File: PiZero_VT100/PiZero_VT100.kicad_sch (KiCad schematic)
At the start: 32 parts, among them J1 GPIO, J2 RS232, J3 Ext. Power max,. 9V DC/AC, J4 Mini-DIN-6, J5 to Testpins 22(DM) and TP23(D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, J6 USB_A, J7 Z80-MBC2 direct, J8 LCD Power, J9 On / Off, K1 G5V-2, Q1 BC547, U1 LM350_TO220

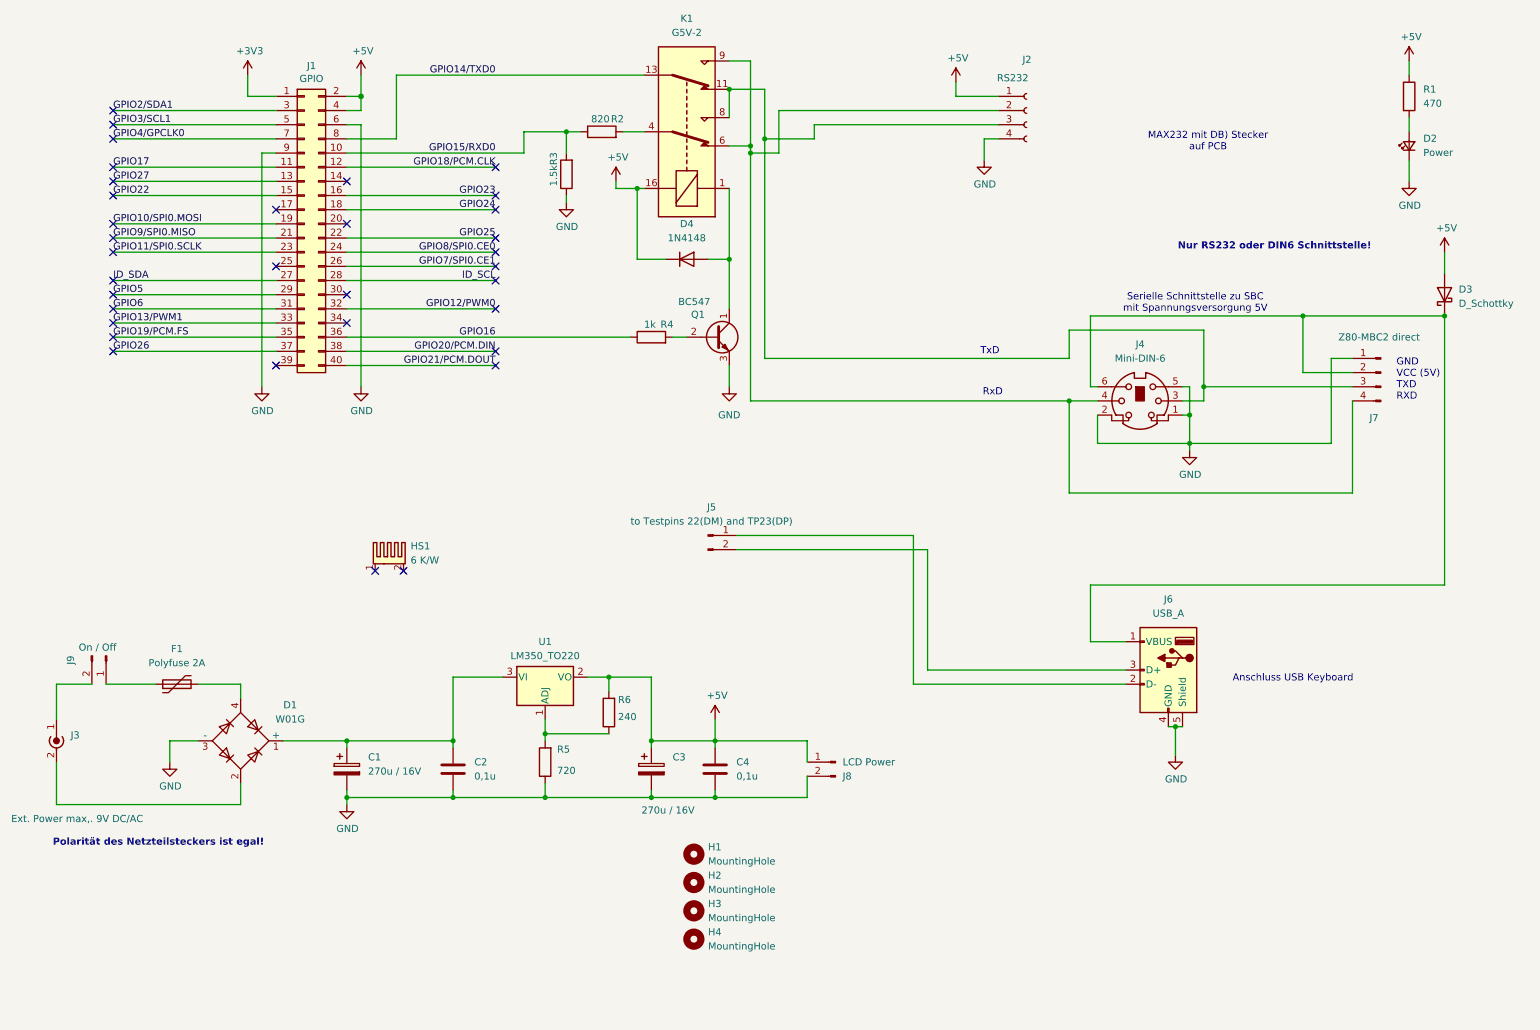
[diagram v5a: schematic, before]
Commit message: Summer berücksichtig Layout für Fertigung bei PCBWays
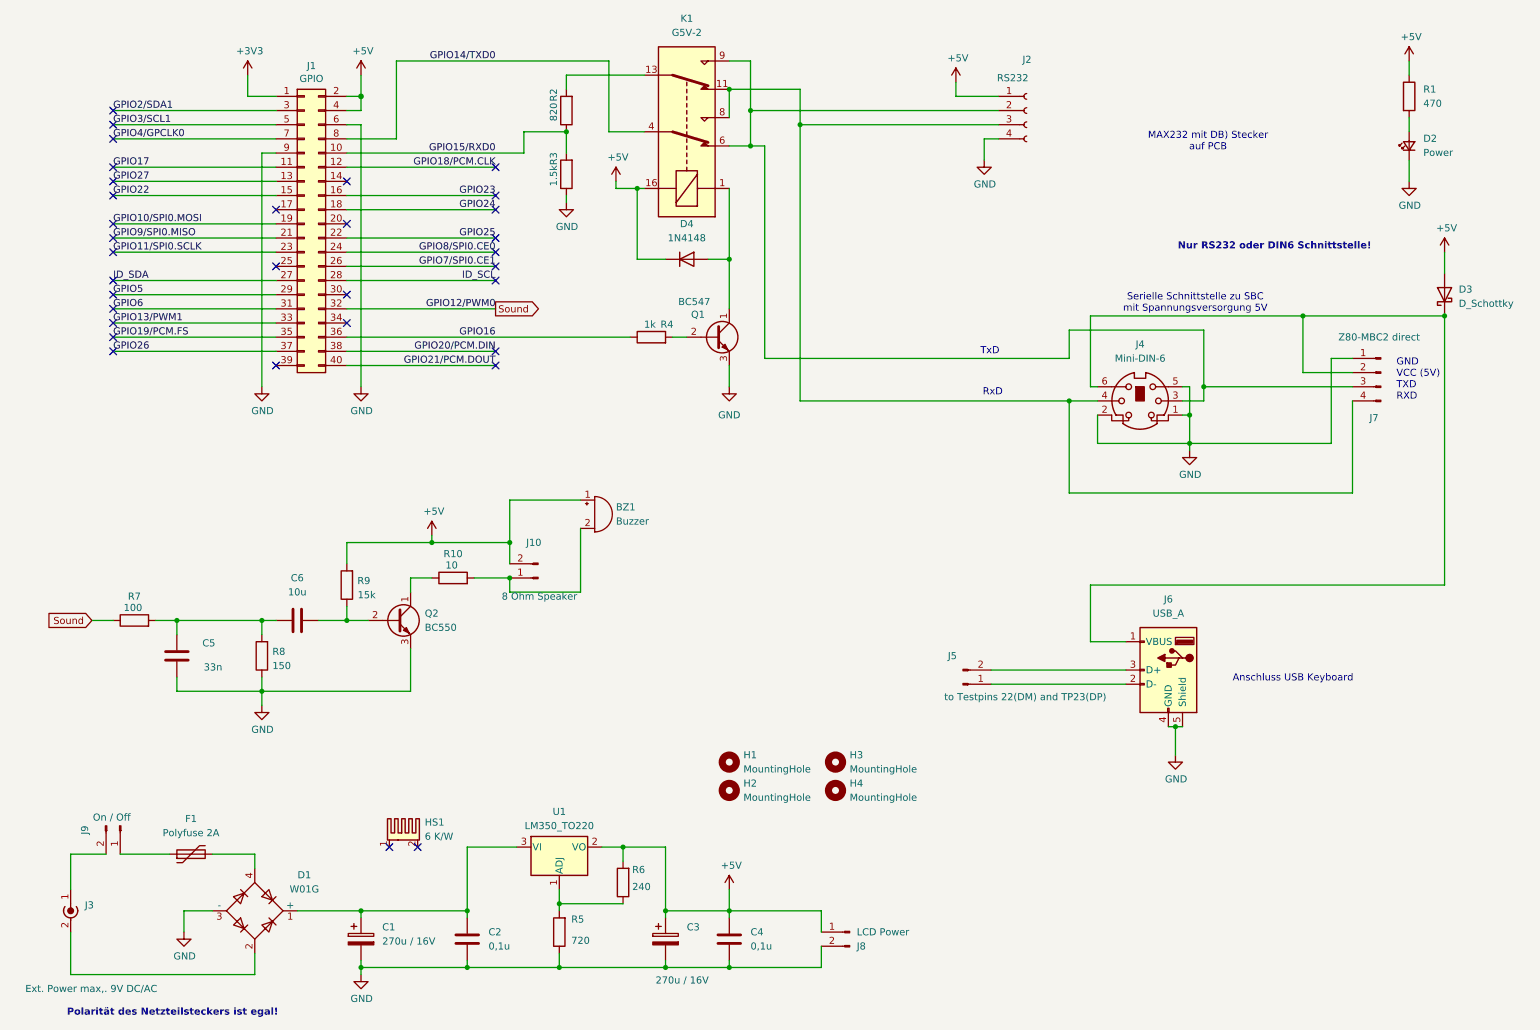
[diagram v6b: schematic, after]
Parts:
- added BZ1: Buzzer, Buzzer_Beeper:Buzzer_TDK_PS1240P02BT_D12.2mm_H6.5mm, symbol Device:Buzzer
- added C5: 33n, Capacitor_THT:C_Rect_L7.0mm_W4.5mm_P5.00mm, symbol Device:C
- added C6: 10u, Capacitor_THT:C_Rect_L9.0mm_W2.6mm_P7.50mm_MKT, symbol Device:C
- added J10: 8 Ohm Speaker, Connector_PinHeader_2.54mm:PinHeader_1x02_P2.54mm_Vertical, symbol Connector:Conn_01x02_Pin
- added Q2: BC550, Package_TO_SOT_THT:TO-92_Wide, symbol Transistor_BJT:BC550
- added R10: 10, Resistor_THT:R_Axial_DIN0207_L6.3mm_D2.5mm_P10.16mm_Horizontal, symbol Device:R
- added R7: 100, Resistor_THT:R_Axial_DIN0207_L6.3mm_D2.5mm_P10.16mm_Horizontal, symbol Device:R
- added R8: 150, Resistor_THT:R_Axial_DIN0207_L6.3mm_D2.5mm_P10.16mm_Horizontal, symbol Device:R
- added R9: 15k, Resistor_THT:R_Axial_DIN0207_L6.3mm_D2.5mm_P10.16mm_Horizontal, symbol Device:R
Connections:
- net +5V: now also BZ1.1 (+), J10.2 (Pin_2), R9.2
- net GND: now also C5.2, Q2.3 (E), R8.1
- net GPIO14/TXD0: now also K1.4; no longer K1.13
- net at J2.2 (Pin_2), K1.6, K1.9: now also J4.3, J7.3 (Pin_3); no longer J4.4, J7.4 (Pin_4)
- net at J2.3 (Pin_3), K1.11, K1.8: now also J4.4, J7.4 (Pin_4); no longer J4.3, J7.3 (Pin_3)
- net at R2.2: now also K1.13; no longer K1.4
- net GPIO12/PWM0 renamed Sound
- net Sound: now also R7.1
- new net: C5.1, C6.1, R7.2, R8.2
- new net: C6.2, Q2.2 (B), R9.1
- new net: BZ1.2 (-), J10.1 (Pin_1), R10.2
- new net: Q2.1 (C), R10.1
- no-connect marks 34 -> 33
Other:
- moved on the sheet: C1, C2, C3, C4, D1, F1, H1, H2, H3, H4, HS1, J3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
